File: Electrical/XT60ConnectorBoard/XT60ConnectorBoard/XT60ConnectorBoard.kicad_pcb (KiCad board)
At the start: 2 copper layers, 17 parts, among them J1 XT60PW-M, J10 XT60PW-M, J11 XT60PW-M, J12 XT60PW-M, J13 XT60PW-M, J2 XT60PW-M, J3 XT60PW-M, J4 XT60PW-M, J5 XT60PW-M, J6 XT60PW-M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

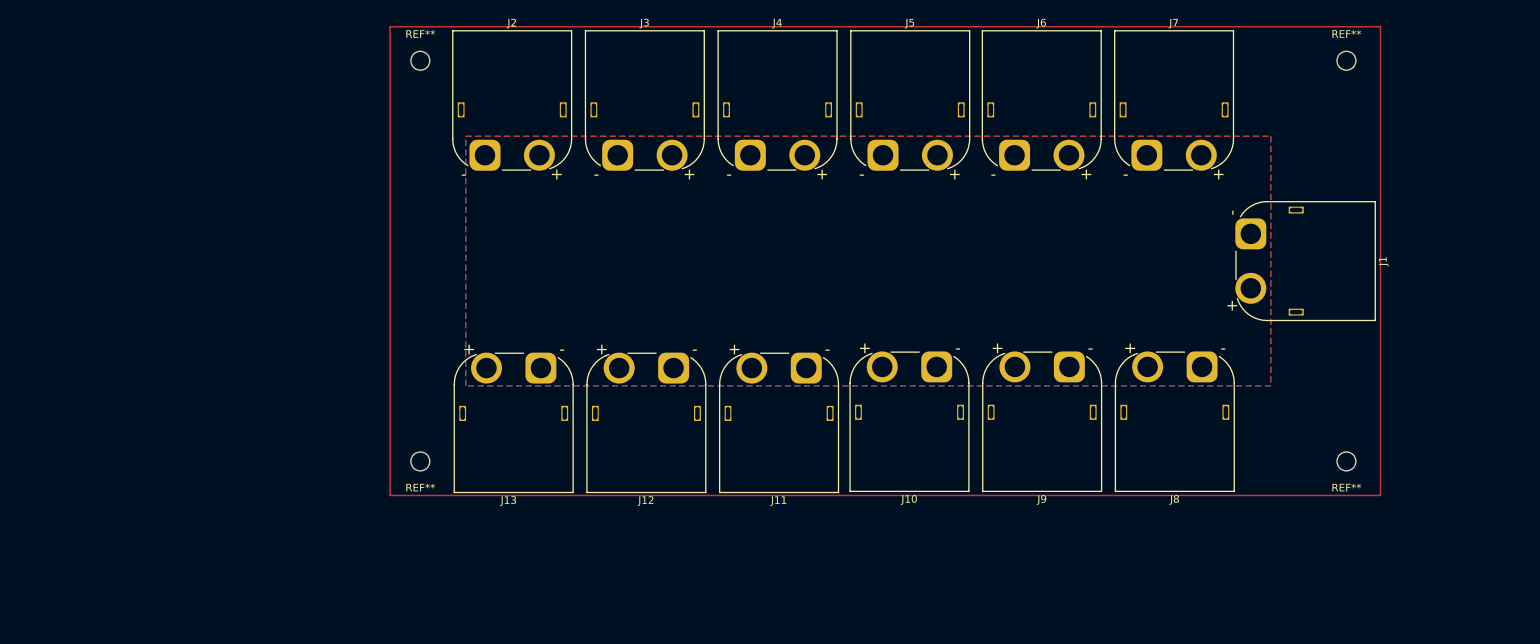
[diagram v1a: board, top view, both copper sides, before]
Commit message: XT60 Board
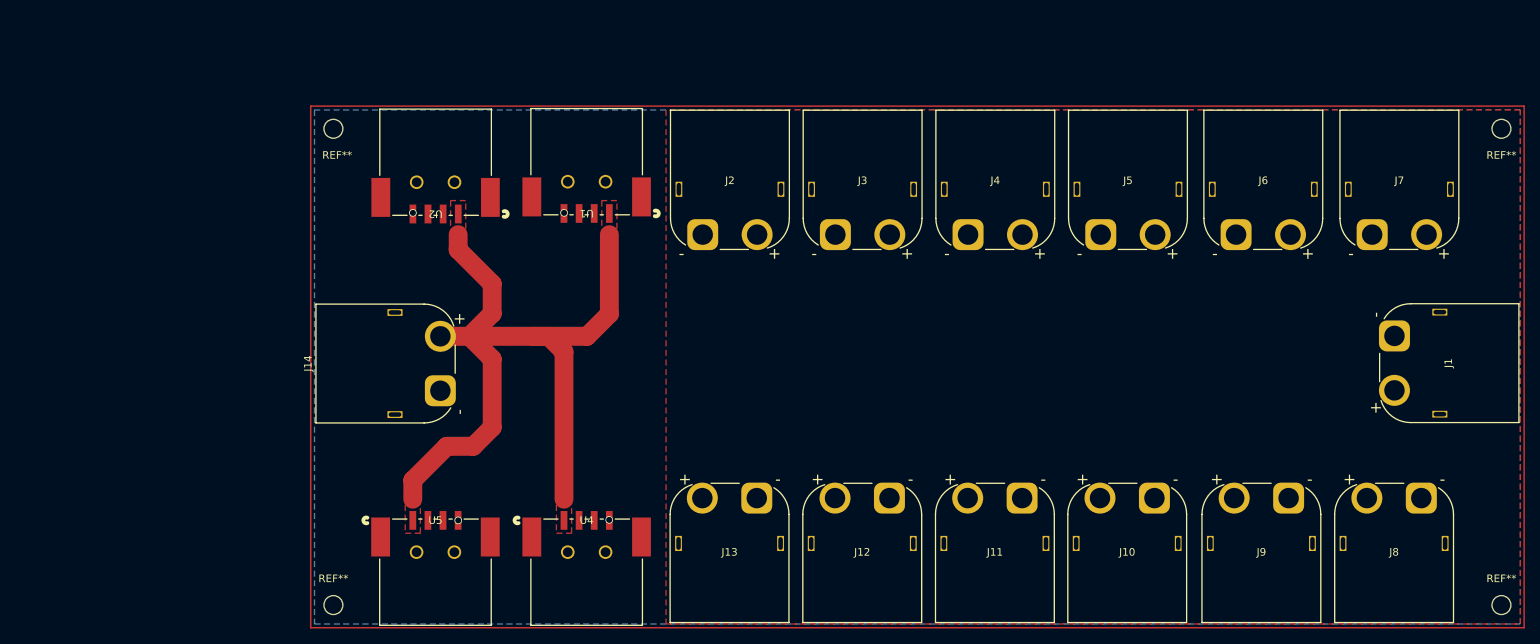
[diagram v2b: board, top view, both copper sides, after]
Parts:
- removed the REF** at (72.5, 57.5)
- removed the REF** at (195.0, 110.5)
- removed the REF** at (72.5, 110.5)
- removed the REF** at (195.0, 57.5)
- added J14: XT60PW-M, Connector_AMASS:AMASS_XT60PW-M_1x02_P7.20mm_Horizontal, F.Cu at (75.2, 101.2)
- added REF**: MountingHole_2.5mm, MountingHole:MountingHole_2.5mm, F.Cu at (61.0, 129.5)
- added REF**: MountingHole_2.5mm, MountingHole:MountingHole_2.5mm, F.Cu at (61.0, 66.5)
- added REF**: MountingHole_2.5mm, MountingHole:MountingHole_2.5mm, F.Cu at (215.5, 66.5)
- added REF**: MountingHole_2.5mm, MountingHole:MountingHole_2.5mm, F.Cu at (215.5, 129.5)
- added U1: USB-A-S-RA-TSMT, _Footprints:USB-A-S-RA-TSMT_ADM, F.Cu at (97.5, 77.7)
- added U2: USB-A-S-RA-TSMT, _Footprints:USB-A-S-RA-TSMT_ADM, F.Cu at (77.5, 77.8)
- added U4: USB-A-S-RA-TSMT, _Footprints:USB-A-S-RA-TSMT_ADM, F.Cu at (91.5, 118.3)
- added U5: USB-A-S-RA-TSMT, _Footprints:USB-A-S-RA-TSMT_ADM, F.Cu at (71.5, 118.3)
- moved J8 33.8 mm to (204.9, 115.3)
- moved J9 33.8 mm to (187.3, 115.3)
- moved J10 33.6 mm to (169.6, 115.3)
- moved J12 33.3 mm to (134.6, 115.3)
- moved J11 33.3 mm to (152.1, 115.3)
- moved J13 33.3 mm to (117.0, 115.3)
- moved J7 31.6 mm to (198.4, 80.5)
- moved J6 31.1 mm to (180.4, 80.5)
- moved J3 30.7 mm to (127.4, 80.5)
- moved J5 30.7 mm to (162.5, 80.5)
- moved J2 30.7 mm to (109.8, 80.5)
- moved J4 30.7 mm to (144.9, 80.5)
- moved J1 23.3 mm to (201.3, 93.9)
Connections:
- net VCC renamed 12+ VCC
- J7 pad 1: unconnected-(J7-+-Pad1) -> GND
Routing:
- net 5+ VCC: track 0.00 -> 104.2 mm
- net GND: vias 0 -> 4
- added copper zone on F.Cu, net 5+ VCC

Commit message: finished xt60 board
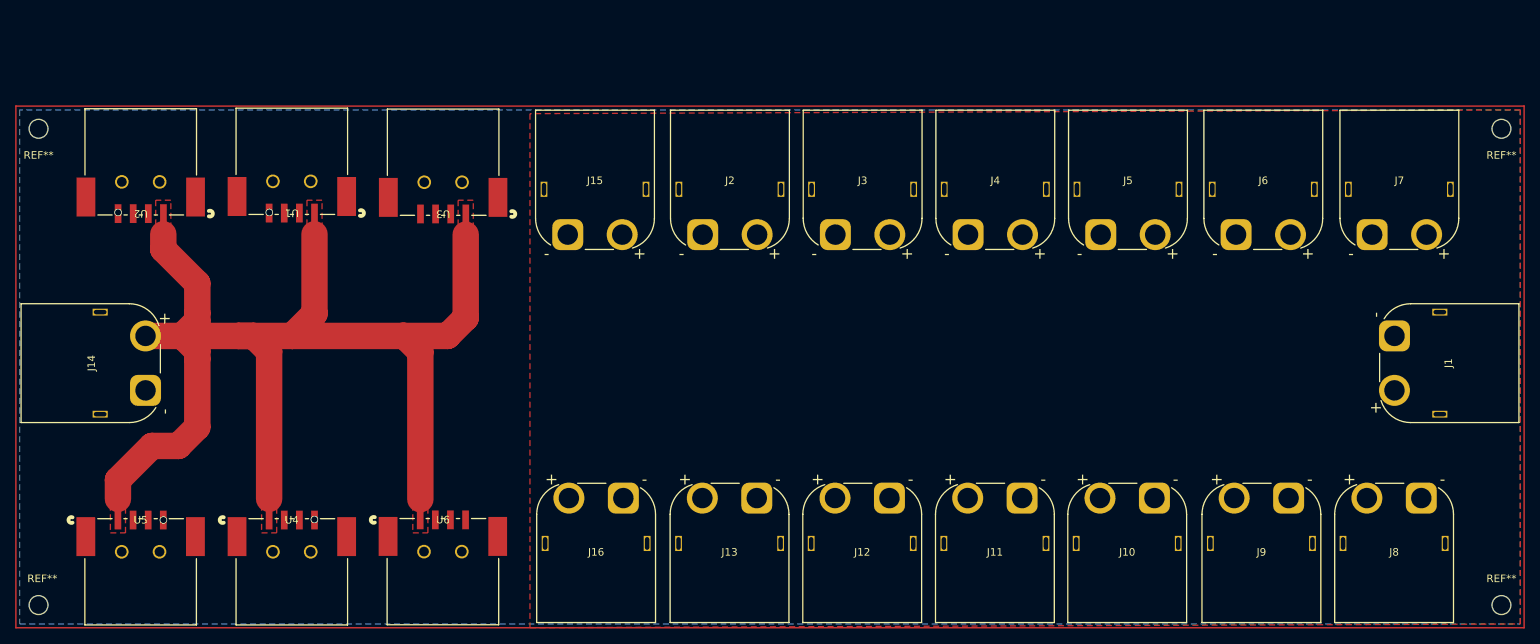
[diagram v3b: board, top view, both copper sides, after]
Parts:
- removed the REF** at (61.0, 129.5)
- removed the REF** at (61.0, 66.5)
- added J15: XT60PW-M, Connector_AMASS:AMASS_XT60PW-M_1x02_P7.20mm_Horizontal, F.Cu at (92.0, 80.5)
- added J16: XT60PW-M, Connector_AMASS:AMASS_XT60PW-M_1x02_P7.20mm_Horizontal, F.Cu at (99.3, 115.3)
- added REF**: MountingHole_2.5mm, MountingHole:MountingHole_2.5mm, F.Cu at (22.0, 66.5)
- added REF**: MountingHole_2.5mm, MountingHole:MountingHole_2.5mm, F.Cu at (22.0, 129.5)
- added U3: USB-A-S-RA-TSMT, _Footprints:USB-A-S-RA-TSMT_ADM, F.Cu at (78.5, 77.8)
- added U6: USB-A-S-RA-TSMT, _Footprints:USB-A-S-RA-TSMT_ADM, F.Cu at (72.5, 118.2)
- moved J14 39.0 mm to (36.1, 101.1)
- moved U1 39.0 mm to (58.5, 77.6)
- moved U2 39.0 mm to (38.5, 77.7)
- moved U4 39.0 mm to (52.5, 118.3)
- moved U5 39.0 mm to (32.5, 118.3)
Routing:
- net 5+ VCC: track 104.2 -> 161.1 mm

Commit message: xt60board
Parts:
- removed J13, J2, J3, J7, J8, J9: XT60PW-M, Connector_AMASS:AMASS_XT60PW-M_1x02_P7.20mm_Horizontal
- removed the REF** at (22.0, 66.5)
- removed the REF** at (22.0, 129.5)
- removed the REF** at (215.5, 66.5)
- removed the REF** at (215.5, 129.5)
- removed U1, U2, U3, U4, U5, U6: USB-A-S-RA-TSMT, _Footprints:USB-A-S-RA-TSMT_ADM
- added REF**: MountingHole_2.5mm, MountingHole:MountingHole_2.5mm, F.Cu at (103.5, 123.5)
- added REF**: MountingHole_2.5mm, MountingHole:MountingHole_2.5mm, F.Cu at (103.5, 60.0)
- added REF**: MountingHole_2.5mm, MountingHole:MountingHole_2.5mm, F.Cu at (182.0, 60.0)
- added REF**: MountingHole_2.5mm, MountingHole:MountingHole_2.5mm, F.Cu at (182.0, 123.5)
- moved J14 101.5 mm to (137.3, 109.5), turned to 180 degrees
- moved J1 90.7 mm to (112.8, 74.2), turned to 0 degrees
- moved J15 40.1 mm to (119.8, 109.5), turned to 180 degrees
- moved J10 27.5 mm to (167.8, 87.9), turned to -90 degrees
- moved J16 27.3 mm to (117.7, 95.1), turned to 90 degrees
- moved J11 21.1 mm to (172.4, 109.5)
- moved J12 21.1 mm to (154.8, 109.5)
- moved J6 16.2 mm to (165.4, 74.2)
- moved J4 15.9 mm to (130.3, 74.2)
- moved J5 15.9 mm to (147.9, 74.2)
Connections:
- J14 pad 2: 5+ VCC -> 12+ VCC
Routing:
- net 5+ VCC: track 161.1 -> 0.00 mm
- net GND: vias 4 -> 0
- removed copper zone on F.Cu, net 5+ VCC
